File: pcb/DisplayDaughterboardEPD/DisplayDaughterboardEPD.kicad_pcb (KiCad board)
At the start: 2 copper layers, 34.8 x 38.9 mm, 24 parts, among them J1 Conn_01x10_Female, J2 Conn_01x24_Female, Q1 SI1308

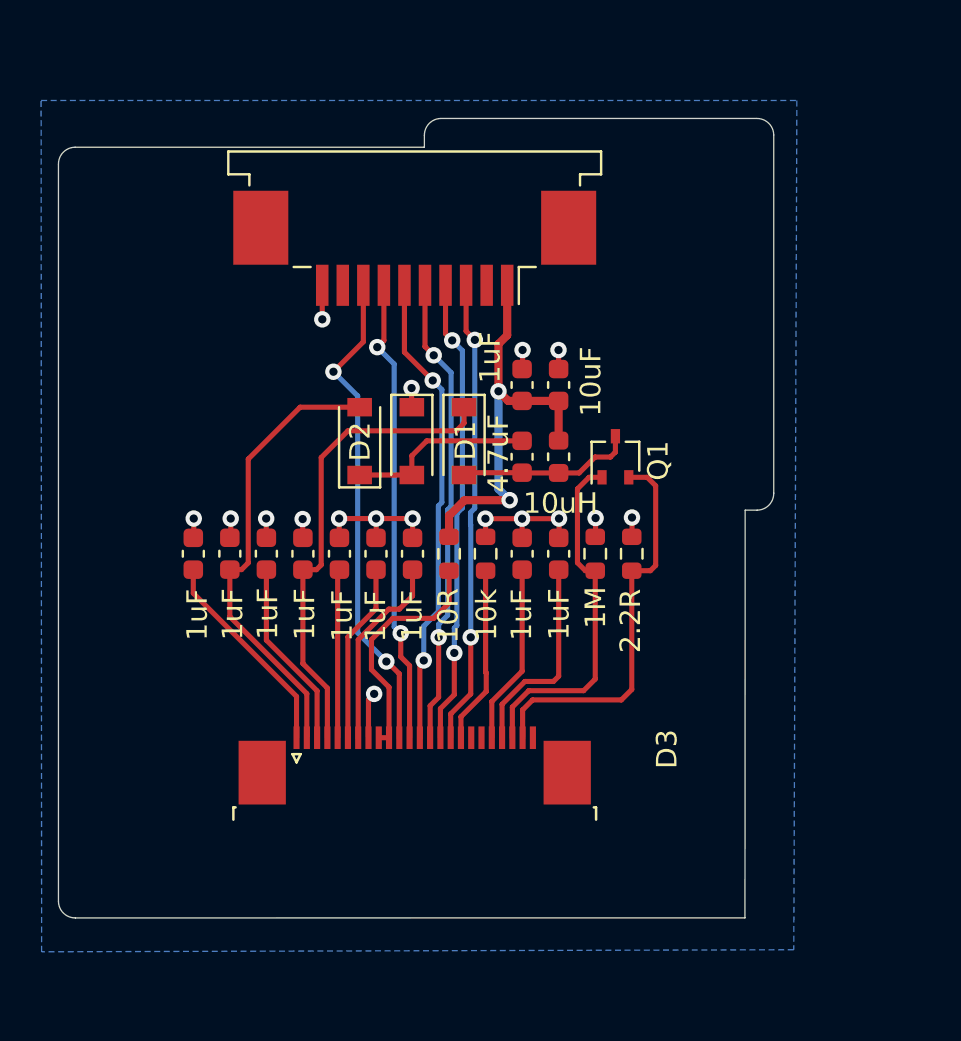
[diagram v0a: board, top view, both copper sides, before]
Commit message: daughterboard update for prod rev2
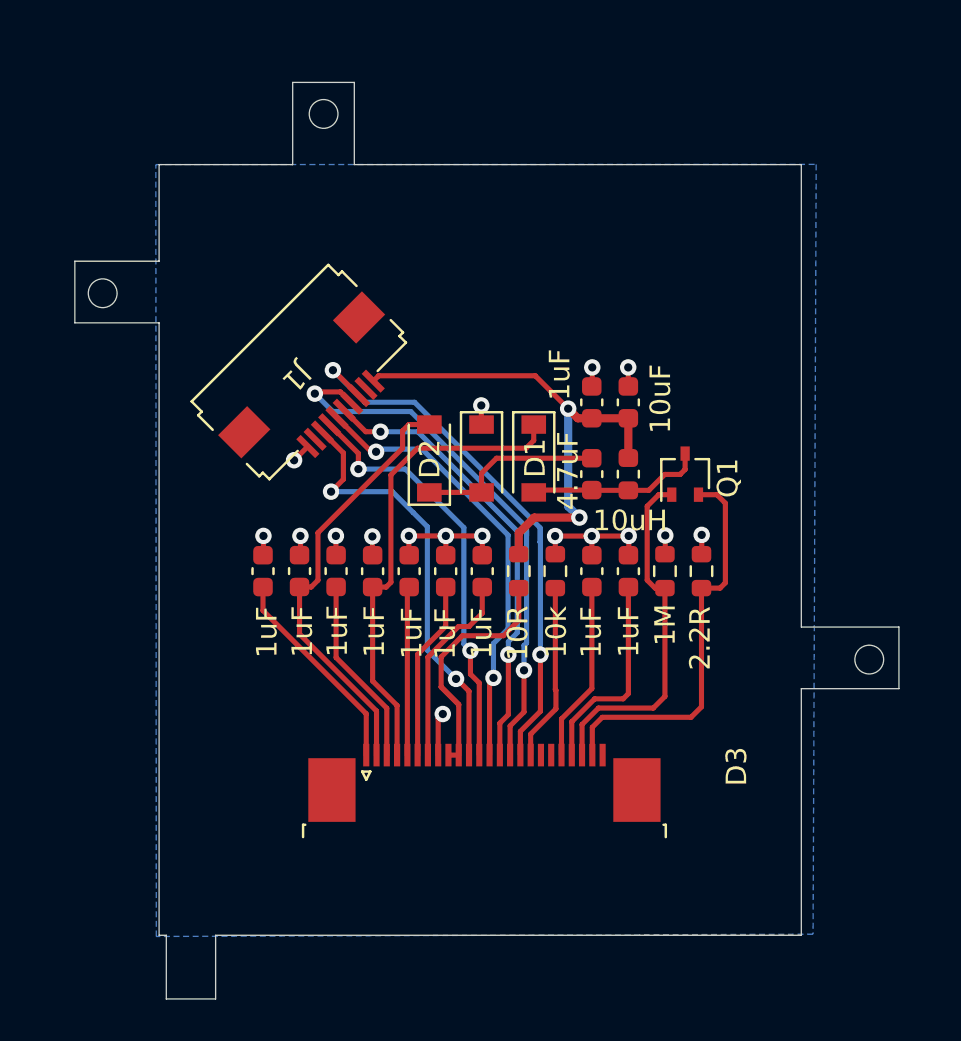
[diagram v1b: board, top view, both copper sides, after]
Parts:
- J1: footprint Connector_FFC-FPC:TE_1-84953-0_1x10-1MP_P1.0mm_Horizontal -> weteor:FCC 1x10 - JUSHUO AFC01-S10FCA-00
- moved J1 8.83 mm to (82.3, 90.5), turned to -135 degrees
- moved C11 3.50 mm to (89.2, 98.1)
- moved C10 3.50 mm to (78.5, 98.1)
- moved C2 3.50 mm to (96.3, 89.9)
- moved C6 3.50 mm to (94.5, 98.1)
- moved D1 3.50 mm to (89.2, 92.6)
- moved L1 3.50 mm to (96.3, 93.4)
- moved R4 3.50 mm to (91.0, 98.1)
- moved C7 3.50 mm to (82.1, 98.1)
- moved D2 3.50 mm to (86.6, 92.6)
- moved C5 3.50 mm to (83.9, 98.1)
- moved R3 3.50 mm to (92.8, 98.1)
- moved C1 3.50 mm to (94.5, 89.9)
- moved C12 3.50 mm to (87.4, 98.1)
- moved C3 3.50 mm to (94.5, 93.4)
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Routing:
- net +3V3: track 20.2 -> 25.1 mm
- net /BUSY: track 22.7 -> 27.1 mm
- net /RESET: track 22.8 -> 26.7 mm
- net /MOSI: track 24.0 -> 20.9 mm
- net /SCLK: track 22.8 -> 20.4 mm
- net /CS: track 23.2 -> 21.9 mm
- net Net-(J2-Pad10): track 11.7 -> 12.9 mm
- net Net-(C9-Pad1): track 22.3 -> 21.2 mm
- net GND: track 25.0 -> 24.1 mm
- net /D/C: track 23.0 -> 22.1 mm
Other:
- board size 34.8 x 38.9 mm -> 40.1 x 44.6 mm

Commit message: change display board to allow for more room above connectors
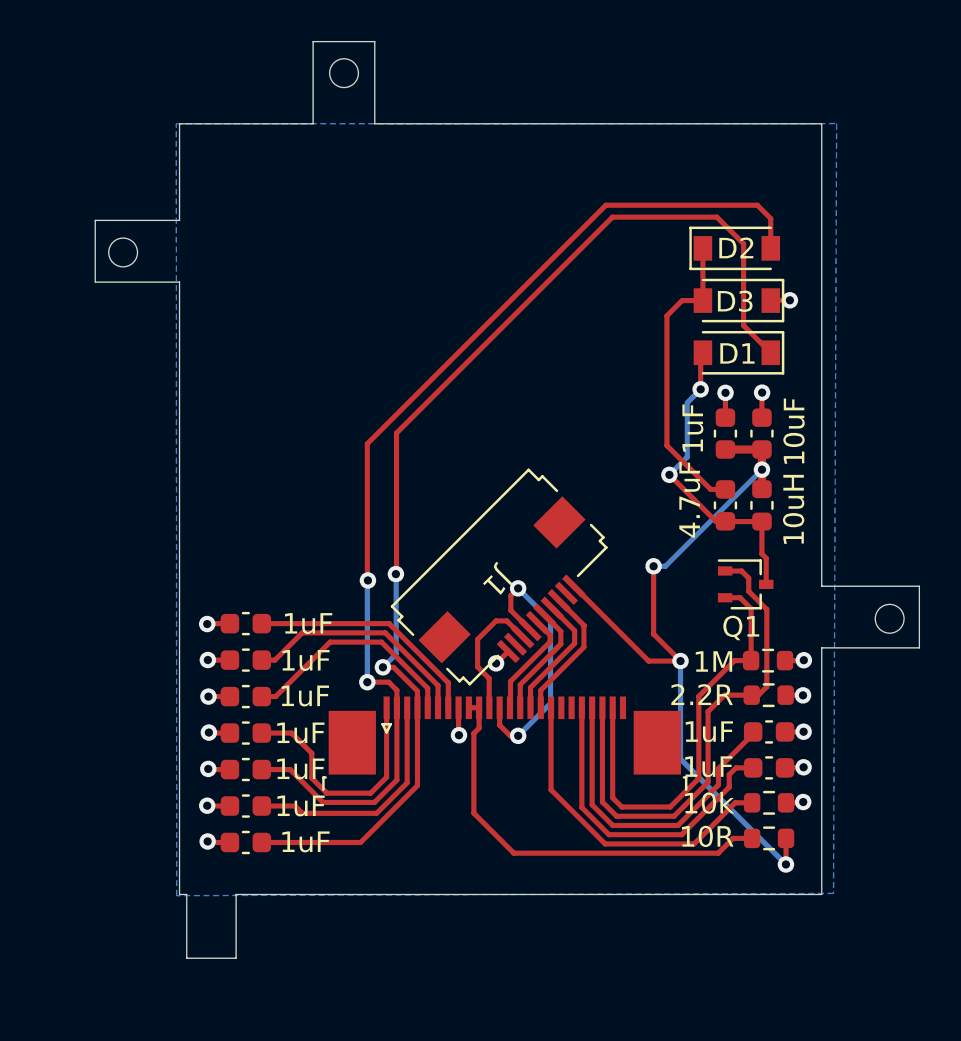
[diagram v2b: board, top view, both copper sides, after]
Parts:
- moved D2 18.1 mm to (101.6, 82.4), turned to 0 degrees
- moved R4 17.8 mm to (103.2, 111.1), turned to 0 degrees
- moved R3 15.3 mm to (103.2, 109.4), turned to 180 degrees
- moved D1 14.6 mm to (101.6, 85.0), turned to 180 degrees
- moved C5 14.6 mm to (77.7, 111.3), turned to 180 degrees
- moved J1 13.9 mm to (92.1, 100.4)
- moved C6 12.9 mm to (103.2, 107.7), turned to 180 degrees
- moved C7 12.2 mm to (77.7, 109.6), turned to 180 degrees
- moved C11 11.8 mm to (77.7, 100.7), turned to 0 degrees
- moved D3 11.1 mm to (101.6, 87.5), turned to 180 degrees
- moved C12 10.6 mm to (77.7, 102.5), turned to 0 degrees
- moved C8 10.4 mm to (103.2, 106.0), turned to 180 degrees
- moved C4 10.0 mm to (77.7, 104.2), turned to 180 degrees
- moved C9 10.0 mm to (77.7, 107.8), turned to 180 degrees
- moved C10 7.92 mm to (77.7, 106.0), turned to 180 degrees
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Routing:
- net Net-(C5-Pad1): track 23.3 -> 54.8 mm, vias 0 -> 2
- net Net-(C9-Pad1): track 21.2 -> 51.4 mm, vias 0 -> 2
- net /BUSY: track 27.1 -> 6.59 mm, vias 2 -> 0
- net /RESET: track 26.7 -> 6.20 mm, vias 2 -> 0
- net /CS: track 21.9 -> 5.22 mm, vias 2 -> 0
- net /D/C: track 22.1 -> 6.23 mm, vias 2 -> 0
- net /MOSI: track 20.9 -> 6.46 mm, vias 2 -> 0
- net +3V3: track 25.1 -> 36.1 mm, vias 2 -> 4
- net Net-(J2-Pad10): track 12.9 -> 20.4 mm
- net /SCLK: track 20.4 -> 13.0 mm
- net Net-(J2-Pad17): track 8.65 -> 15.7 mm
- net /RESE: track 17.4 -> 24.4 mm
- net Net-(C6-Pad2): track 8.79 -> 15.4 mm
- net Net-(C3-Pad2): track 8.61 -> 15.2 mm, vias 0 -> 2
- net GND: track 24.1 -> 17.5 mm
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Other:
- outline, holes or cut-outs redrawn

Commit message: unsaved changes
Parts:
- L1: footprint Inductor_SMD:L_0603_1608Metric -> Inductor_SMD:L_1210_3225Metric
- Q1: value SI1308 -> AO3400A; footprint Package_TO_SOT_SMD:SOT-323_SC-70 -> Package_TO_SOT_SMD:SOT-23
- R1: value 2.2R -> 0.47R
- moved C1 6.57 mm to (98.1, 97.3), turned to 180 degrees
- moved D2 6.49 mm to (100.9, 88.9), turned to 90 degrees
- moved C2 6.32 mm to (98.1, 95.6), turned to 180 degrees
- moved D1 4.33 mm to (103.5, 88.9), turned to -90 degrees
- moved D3 3.53 mm to (98.3, 88.9), turned to -90 degrees
- moved C3 3.17 mm to (99.1, 92.4), turned to 180 degrees
- moved Q1 0.94 mm to (102.7, 99.4)
- moved L1 0.83 mm to (102.3, 95.6), turned to 0 degrees
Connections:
- Q1 pad 1: /RESE -> Net-(J2-Pad23)
- Q1 pad 2: Net-(J2-Pad23) -> /RESE
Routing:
- net Net-(C5-Pad1): track 54.8 -> 41.7 mm
- net Net-(C3-Pad1): track 14.6 -> 5.24 mm
- net Net-(C9-Pad1): track 51.4 -> 44.3 mm
- net +3V3: track 36.1 -> 29.0 mm, vias 4 -> 2
- net /RESE: track 24.4 -> 22.1 mm
- net Net-(J2-Pad23): track 20.6 -> 22.8 mm
- net Net-(C3-Pad2): track 15.2 -> 13.9 mm, vias 2 -> 0

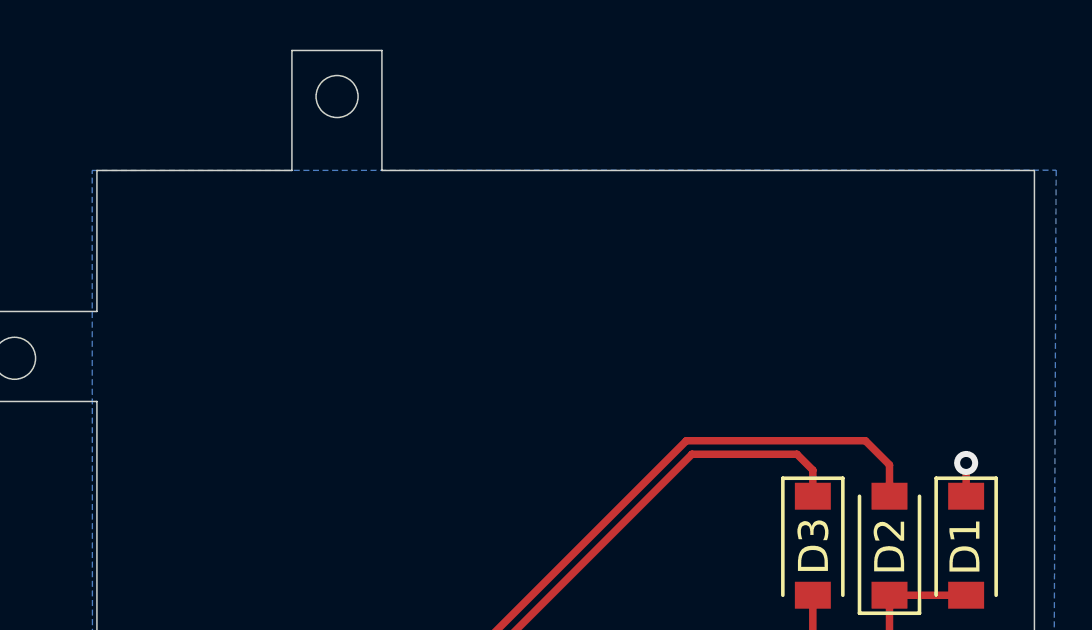
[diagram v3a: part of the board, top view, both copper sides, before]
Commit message: add license print to front silkscreen
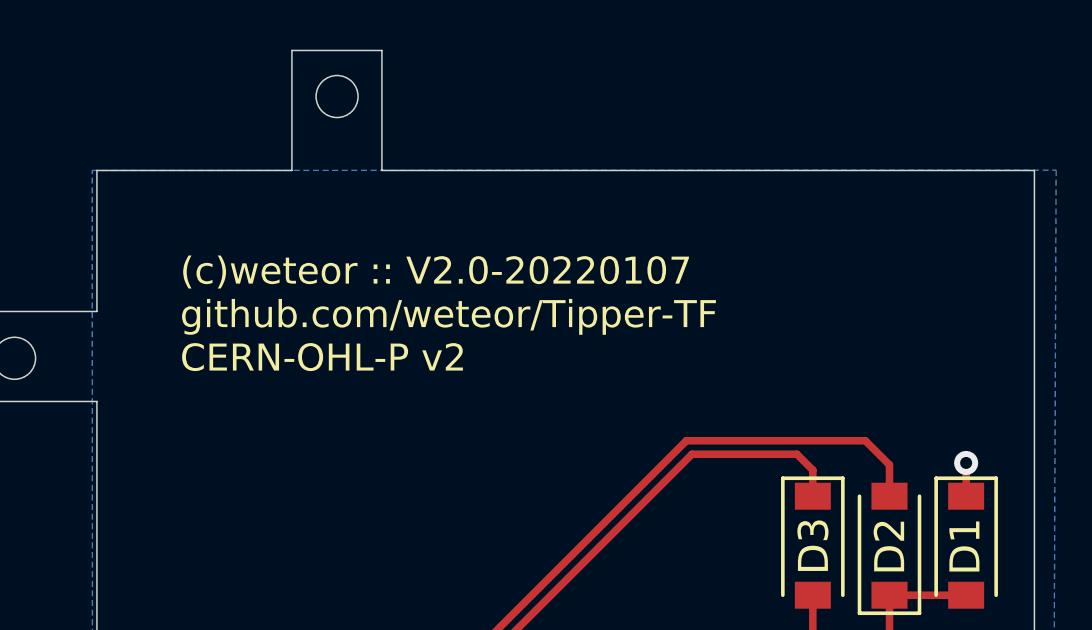
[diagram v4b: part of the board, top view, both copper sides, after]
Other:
- board text added: "(c)weteor :: V2.0-20220107 github.com/weteor/Tipper-TF CERN-OHL-P v2"
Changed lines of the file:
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@@
   (gr_circle (center 82.490971 73.896056) (end 83.190972 73.896054) (layer "Edge.Cuts") (width 0.05) (fill none))
   (gr_line (start 80.985971 76.361054) (end 80.985971 72.361054) (layer "Edge.Cuts") (width 0.05))
+  (gr_text "(c)weteor :: V2.0-20220107\ngithub.com/weteor/Tipper-TF\nCERN-OHL-P v2" (at 77.255 81.165) (layer "F.SilkS")
+    (effects (font (size 0.9 0.9) (thickness 0.153)) (justify left))
+  )
   (segment (start 98.855 95.6) (end 100.92 95.6) (width 0.25) (layer "F.Cu") (net 1))
   (segment (start 98.864047 102.501734) (end 98.864047 97.302047) (width 0.25) (layer "F.Cu") (net 1))
